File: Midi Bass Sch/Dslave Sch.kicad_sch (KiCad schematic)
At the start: 12 parts, among them J6 D SLAVE ISCP, SW5 D-slave Reset, U7 PIC16F1789

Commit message: working on troubleshooting section of report
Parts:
- renumbered J6 to J7, R50 to R62, R51 to R63, R52 to R64, R53 to R65, U7 to U9
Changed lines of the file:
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@@
 		(dnp no)
 		(fields_autoplaced yes)
-		(property "Reference" "R51"
+		(property "Reference" "R63"
 			(at 50.8 125.7299 90)
 			(effects
@@
 			(project "Midi Bass Sch"
 				(path "/06818073-fb22-48ee-acc5-6dedd827034e/4e89443f-252f-4d60-96aa-3cd5b0237902"
-					(reference "R51")
+					(reference "R63")
 					(unit 1)
 				)
@@
 		(on_board yes)
 		(dnp no)
-		(property "Reference" "U7"
+		(property "Reference" "U9"
 			(at 114.808 26.67 0)
 			(effects
@@
 			(project "Midi Bass Sch"
 				(path "/06818073-fb22-48ee-acc5-6dedd827034e/4e89443f-252f-4d60-96aa-3cd5b0237902"
-					(reference "U7")
+					(reference "U9")
 					(unit 1)
 				)
@@
 		(dnp no)
 		(fields_autoplaced yes)
-		(property "Reference" "#PWR080"
+		(property "Reference" "#PWR094"
 			(at 190.5 124.46 0)
 			(effects
@@
 			(project "Midi Bass Sch"
 				(path "/06818073-fb22-48ee-acc5-6dedd827034e/4e89443f-252f-4d60-96aa-3cd5b0237902"
-					(reference "#PWR080")
+					(reference "#PWR094")
 					(unit 1)
 				)
@@
 		(dnp no)
 		(fields_autoplaced yes)
-		(property "Reference" "#PWR078"
+		(property "Reference" "#PWR092"
 			(at 110.1344 21.6916 0)
 			(effects
@@
 			(project "Midi Bass Sch"
 				(path "/06818073-fb22-48ee-acc5-6dedd827034e/4e89443f-252f-4d60-96aa-3cd5b0237902"
-					(reference "#PWR078")
+					(reference "#PWR092")
 					(unit 1)
 				)
@@
 		(dnp no)
 		(fields_autoplaced yes)
-		(property "Reference" "#PWR073"
+		(property "Reference" "#PWR087"
 			(at 40.2844 59.7916 0)
 			(effects
@@
 			(project "Midi Bass Sch"
 				(path "/06818073-fb22-48ee-acc5-6dedd827034e/4e89443f-252f-4d60-96aa-3cd5b0237902"
-					(reference "#PWR073")
+					(reference "#PWR087")
 					(unit 1)
 				)
@@
 		(dnp no)
 		(fields_autoplaced yes)
-		(property "Reference" "R52"
+		(property "Reference" "R64"
 			(at 179.07 113.0299 90)
 			(effects
@@
 			(project "Midi Bass Sch"
 				(path "/06818073-fb22-48ee-acc5-6dedd827034e/4e89443f-252f-4d60-96aa-3cd5b0237902"
-					(reference "R52")
+					(reference "R64")
 					(unit 1)
 				)
@@
 		(dnp no)
 		(fields_autoplaced yes)
-		(property "Reference" "#PWR077"
+		(property "Reference" "#PWR091"
 			(at 102.87 158.75 0)
 			(effects
@@
 			(project "Midi Bass Sch"
 				(path "/06818073-fb22-48ee-acc5-6dedd827034e/4e89443f-252f-4d60-96aa-3cd5b0237902"
-					(reference "#PWR077")
+					(reference "#PWR091")
 					(unit 1)
 				)
@@
 		(dnp no)
 		(fields_autoplaced yes)
-		(property "Reference" "#PWR074"
+		(property "Reference" "#PWR088"
 			(at 35.56 72.39 0)
 			(effects
@@
 			(project "Midi Bass Sch"
 				(path "/06818073-fb22-48ee-acc5-6dedd827034e/4e89443f-252f-4d60-96aa-3cd5b0237902"
-					(reference "#PWR074")
+					(reference "#PWR088")
 					(unit 1)
 				)
@@
 		(dnp no)
 		(fields_autoplaced yes)
-		(property "Reference" "R53"
+		(property "Reference" "R65"
 			(at 193.04 110.4899 90)
 			(effects
@@
 			(project "Midi Bass Sch"
 				(path "/06818073-fb22-48ee-acc5-6dedd827034e/4e89443f-252f-4d60-96aa-3cd5b0237902"
-					(reference "R53")
+					(reference "R65")
 					(unit 1)
 				)
@@
 		(dnp no)
 		(fields_autoplaced yes)
-		(property "Reference" "R50"
+		(property "Reference" "R62"
 			(at 29.21 137.1599 90)
 			(effects
@@
 			(project "Midi Bass Sch"
 				(path "/06818073-fb22-48ee-acc5-6dedd827034e/4e89443f-252f-4d60-96aa-3cd5b0237902"
-					(reference "R50")
+					(reference "R62")
 					(unit 1)
 				)
@@
 		(dnp no)
 		(fields_autoplaced yes)
-		(property "Reference" "#PWR076"
+		(property "Reference" "#PWR090"
 			(at 48.26 139.7 0)
 			(effects
@@
 			(project "Midi Bass Sch"
 				(path "/06818073-fb22-48ee-acc5-6dedd827034e/4e89443f-252f-4d60-96aa-3cd5b0237902"
-					(reference "#PWR076")
+					(reference "#PWR090")
 					(unit 1)
 				)
@@
 		(dnp no)
 		(fields_autoplaced yes)
-		(property "Reference" "J6"
+		(property "Reference" "J7"
 			(at 24.13 59.69 0)
 			(effects
@@
 			(project "Midi Bass Sch"
 				(path "/06818073-fb22-48ee-acc5-6dedd827034e/4e89443f-252f-4d60-96aa-3cd5b0237902"
-					(reference "J6")
+					(reference "J7")
 					(unit 1)
 				)
@@
 		(dnp no)
 		(fields_autoplaced yes)
-		(property "Reference" "#PWR079"
+		(property "Reference" "#PWR093"
 			(at 176.53 127 0)
 			(effects
@@
 			(project "Midi Bass Sch"
 				(path "/06818073-fb22-48ee-acc5-6dedd827034e/4e89443f-252f-4d60-96aa-3cd5b0237902"
-					(reference "#PWR079")
+					(reference "#PWR093")
 					(unit 1)
 				)
@@
 		(dnp no)
 		(fields_autoplaced yes)
-		(property "Reference" "#PWR075"
+		(property "Reference" "#PWR089"
 			(at 52.9844 118.2116 0)
 			(effects
@@
 			(project "Midi Bass Sch"
 				(path "/06818073-fb22-48ee-acc5-6dedd827034e/4e89443f-252f-4d60-96aa-3cd5b0237902"
-					(reference "#PWR075")
+					(reference "#PWR089")
 					(unit 1)
 				)
@@
 		(dnp no)
 		(fields_autoplaced yes)
-		(property "Reference" "#PWR072"
+		(property "Reference" "#PWR086"
 			(at 26.67 140.97 0)
 			(effects
@@
 			(project "Midi Bass Sch"
 				(path "/06818073-fb22-48ee-acc5-6dedd827034e/4e89443f-252f-4d60-96aa-3cd5b0237902"
-					(reference "#PWR072")
-					(unit 1)
-				)
+					(reference "#PWR086")
+					(unit 1)
+				)

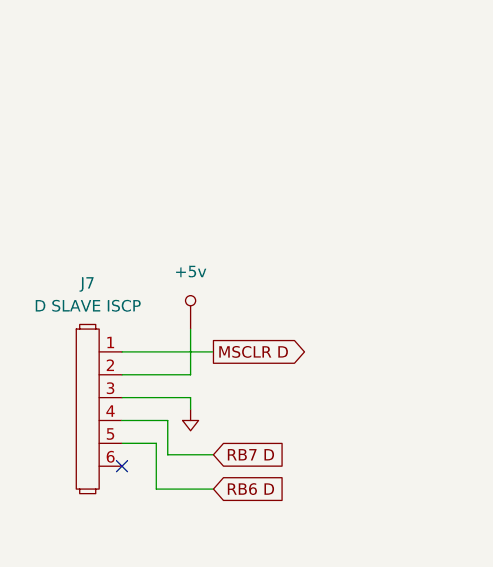
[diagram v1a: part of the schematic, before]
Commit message: working on final troubleshooting sections, modified pluck slave to header connections
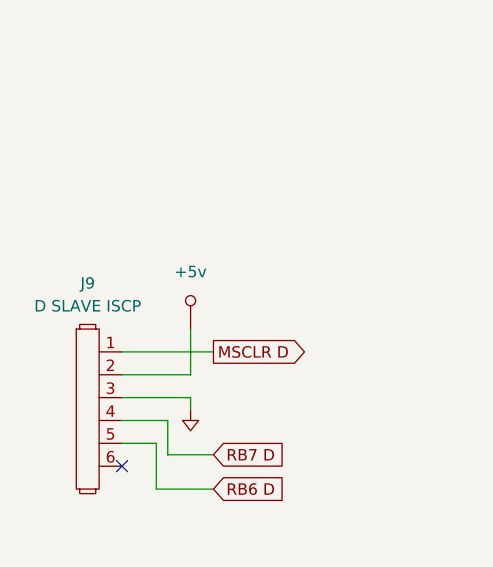
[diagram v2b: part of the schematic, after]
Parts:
- renumbered J7 to J9
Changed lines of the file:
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@@
 		(dnp no)
 		(fields_autoplaced yes)
-		(property "Reference" "#PWR094"
+		(property "Reference" "#PWR096"
 			(at 190.5 124.46 0)
 			(effects
@@
 			(project "Midi Bass Sch"
 				(path "/06818073-fb22-48ee-acc5-6dedd827034e/4e89443f-252f-4d60-96aa-3cd5b0237902"
-					(reference "#PWR094")
+					(reference "#PWR096")
 					(unit 1)
 				)
@@
 		(dnp no)
 		(fields_autoplaced yes)
-		(property "Reference" "#PWR092"
+		(property "Reference" "#PWR094"
 			(at 110.1344 21.6916 0)
 			(effects
@@
 			(project "Midi Bass Sch"
 				(path "/06818073-fb22-48ee-acc5-6dedd827034e/4e89443f-252f-4d60-96aa-3cd5b0237902"
-					(reference "#PWR092")
+					(reference "#PWR094")
 					(unit 1)
 				)
@@
 		(dnp no)
 		(fields_autoplaced yes)
-		(property "Reference" "#PWR087"
+		(property "Reference" "#PWR089"
 			(at 40.2844 59.7916 0)
 			(effects
@@
 			(project "Midi Bass Sch"
 				(path "/06818073-fb22-48ee-acc5-6dedd827034e/4e89443f-252f-4d60-96aa-3cd5b0237902"
-					(reference "#PWR087")
+					(reference "#PWR089")
 					(unit 1)
 				)
@@
 		(dnp no)
 		(fields_autoplaced yes)
-		(property "Reference" "#PWR091"
+		(property "Reference" "#PWR093"
 			(at 102.87 158.75 0)
 			(effects
@@
 			(project "Midi Bass Sch"
 				(path "/06818073-fb22-48ee-acc5-6dedd827034e/4e89443f-252f-4d60-96aa-3cd5b0237902"
-					(reference "#PWR091")
+					(reference "#PWR093")
 					(unit 1)
 				)
@@
 		(dnp no)
 		(fields_autoplaced yes)
-		(property "Reference" "#PWR088"
+		(property "Reference" "#PWR090"
 			(at 35.56 72.39 0)
 			(effects
@@
 			(project "Midi Bass Sch"
 				(path "/06818073-fb22-48ee-acc5-6dedd827034e/4e89443f-252f-4d60-96aa-3cd5b0237902"
-					(reference "#PWR088")
+					(reference "#PWR090")
 					(unit 1)
 				)
@@
 		(dnp no)
 		(fields_autoplaced yes)
-		(property "Reference" "#PWR090"
+		(property "Reference" "#PWR092"
 			(at 48.26 139.7 0)
 			(effects
@@
 			(project "Midi Bass Sch"
 				(path "/06818073-fb22-48ee-acc5-6dedd827034e/4e89443f-252f-4d60-96aa-3cd5b0237902"
-					(reference "#PWR090")
+					(reference "#PWR092")
 					(unit 1)
 				)
@@
 		(dnp no)
 		(fields_autoplaced yes)
-		(property "Reference" "J7"
+		(property "Reference" "J9"
 			(at 24.13 59.69 0)
 			(effects
@@
 			(project "Midi Bass Sch"
 				(path "/06818073-fb22-48ee-acc5-6dedd827034e/4e89443f-252f-4d60-96aa-3cd5b0237902"
-					(reference "J7")
+					(reference "J9")
 					(unit 1)
 				)
@@
 		(dnp no)
 		(fields_autoplaced yes)
-		(property "Reference" "#PWR093"
+		(property "Reference" "#PWR095"
 			(at 176.53 127 0)
 			(effects
@@
 			(project "Midi Bass Sch"
 				(path "/06818073-fb22-48ee-acc5-6dedd827034e/4e89443f-252f-4d60-96aa-3cd5b0237902"
-					(reference "#PWR093")
+					(reference "#PWR095")
 					(unit 1)
 				)
@@
 		(dnp no)
 		(fields_autoplaced yes)
-		(property "Reference" "#PWR089"
+		(property "Reference" "#PWR091"
 			(at 52.9844 118.2116 0)
 			(effects
@@
 			(project "Midi Bass Sch"
 				(path "/06818073-fb22-48ee-acc5-6dedd827034e/4e89443f-252f-4d60-96aa-3cd5b0237902"
-					(reference "#PWR089")
+					(reference "#PWR091")
 					(unit 1)
 				)
@@
 		(dnp no)
 		(fields_autoplaced yes)
-		(property "Reference" "#PWR086"
+		(property "Reference" "#PWR088"
 			(at 26.67 140.97 0)
 			(effects
@@
 			(project "Midi Bass Sch"
 				(path "/06818073-fb22-48ee-acc5-6dedd827034e/4e89443f-252f-4d60-96aa-3cd5b0237902"
-					(reference "#PWR086")
-					(unit 1)
-				)
+					(reference "#PWR088")
+					(unit 1)
+				)

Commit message: finished troubleshooting section
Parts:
- renumbered J9 to J11
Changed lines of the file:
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@@
 		(dnp no)
 		(fields_autoplaced yes)
-		(property "Reference" "#PWR096"
+		(property "Reference" "#PWR098"
 			(at 190.5 124.46 0)
 			(effects
@@
 			(project "Midi Bass Sch"
 				(path "/06818073-fb22-48ee-acc5-6dedd827034e/4e89443f-252f-4d60-96aa-3cd5b0237902"
-					(reference "#PWR096")
+					(reference "#PWR098")
 					(unit 1)
 				)
@@
 		(dnp no)
 		(fields_autoplaced yes)
-		(property "Reference" "#PWR094"
+		(property "Reference" "#PWR096"
 			(at 110.1344 21.6916 0)
 			(effects
@@
 			(project "Midi Bass Sch"
 				(path "/06818073-fb22-48ee-acc5-6dedd827034e/4e89443f-252f-4d60-96aa-3cd5b0237902"
-					(reference "#PWR094")
+					(reference "#PWR096")
 					(unit 1)
 				)
@@
 		(dnp no)
 		(fields_autoplaced yes)
-		(property "Reference" "#PWR089"
+		(property "Reference" "#PWR091"
 			(at 40.2844 59.7916 0)
 			(effects
@@
 			(project "Midi Bass Sch"
 				(path "/06818073-fb22-48ee-acc5-6dedd827034e/4e89443f-252f-4d60-96aa-3cd5b0237902"
-					(reference "#PWR089")
+					(reference "#PWR091")
 					(unit 1)
 				)
@@
 		(dnp no)
 		(fields_autoplaced yes)
-		(property "Reference" "#PWR093"
+		(property "Reference" "#PWR095"
 			(at 102.87 158.75 0)
 			(effects
@@
 			(project "Midi Bass Sch"
 				(path "/06818073-fb22-48ee-acc5-6dedd827034e/4e89443f-252f-4d60-96aa-3cd5b0237902"
-					(reference "#PWR093")
+					(reference "#PWR095")
 					(unit 1)
 				)
@@
 		(dnp no)
 		(fields_autoplaced yes)
-		(property "Reference" "#PWR090"
+		(property "Reference" "#PWR092"
 			(at 35.56 72.39 0)
 			(effects
@@
 			(project "Midi Bass Sch"
 				(path "/06818073-fb22-48ee-acc5-6dedd827034e/4e89443f-252f-4d60-96aa-3cd5b0237902"
-					(reference "#PWR090")
+					(reference "#PWR092")
 					(unit 1)
 				)
@@
 		(dnp no)
 		(fields_autoplaced yes)
-		(property "Reference" "#PWR092"
+		(property "Reference" "#PWR094"
 			(at 48.26 139.7 0)
 			(effects
@@
 			(project "Midi Bass Sch"
 				(path "/06818073-fb22-48ee-acc5-6dedd827034e/4e89443f-252f-4d60-96aa-3cd5b0237902"
-					(reference "#PWR092")
+					(reference "#PWR094")
 					(unit 1)
 				)
@@
 		(dnp no)
 		(fields_autoplaced yes)
-		(property "Reference" "J9"
+		(property "Reference" "J11"
 			(at 24.13 59.69 0)
 			(effects
@@
 			(project "Midi Bass Sch"
 				(path "/06818073-fb22-48ee-acc5-6dedd827034e/4e89443f-252f-4d60-96aa-3cd5b0237902"
-					(reference "J9")
+					(reference "J11")
 					(unit 1)
 				)
@@
 		(dnp no)
 		(fields_autoplaced yes)
-		(property "Reference" "#PWR095"
+		(property "Reference" "#PWR097"
 			(at 176.53 127 0)
 			(effects
@@
 			(project "Midi Bass Sch"
 				(path "/06818073-fb22-48ee-acc5-6dedd827034e/4e89443f-252f-4d60-96aa-3cd5b0237902"
-					(reference "#PWR095")
+					(reference "#PWR097")
 					(unit 1)
 				)
@@
 		(dnp no)
 		(fields_autoplaced yes)
-		(property "Reference" "#PWR091"
+		(property "Reference" "#PWR093"
 			(at 52.9844 118.2116 0)
 			(effects
@@
 			(project "Midi Bass Sch"
 				(path "/06818073-fb22-48ee-acc5-6dedd827034e/4e89443f-252f-4d60-96aa-3cd5b0237902"
-					(reference "#PWR091")
+					(reference "#PWR093")
 					(unit 1)
 				)
@@
 		(dnp no)
 		(fields_autoplaced yes)
-		(property "Reference" "#PWR088"
+		(property "Reference" "#PWR090"
 			(at 26.67 140.97 0)
 			(effects
@@
 			(project "Midi Bass Sch"
 				(path "/06818073-fb22-48ee-acc5-6dedd827034e/4e89443f-252f-4d60-96aa-3cd5b0237902"
-					(reference "#PWR088")
-					(unit 1)
-				)
+					(reference "#PWR090")
+					(unit 1)
+				)

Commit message: began getting images for schematic appendix
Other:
- title: (none) -> D-Slave Processor Schematic
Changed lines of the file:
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@@
 	(generator_version "8.0")
 	(paper "A")
+	(title_block
+		(title "D-Slave Processor Schematic")
+		(date "2024-12-10")
+		(rev "A")
+	)
 	(junction
 		(at 48.26 133.35)
